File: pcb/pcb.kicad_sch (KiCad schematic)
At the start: 22 parts, among them J1 AVR-ISP-6, SW1 BOOT, SW2 RESET, U1 ATmega328P-P, Y1 Crystal

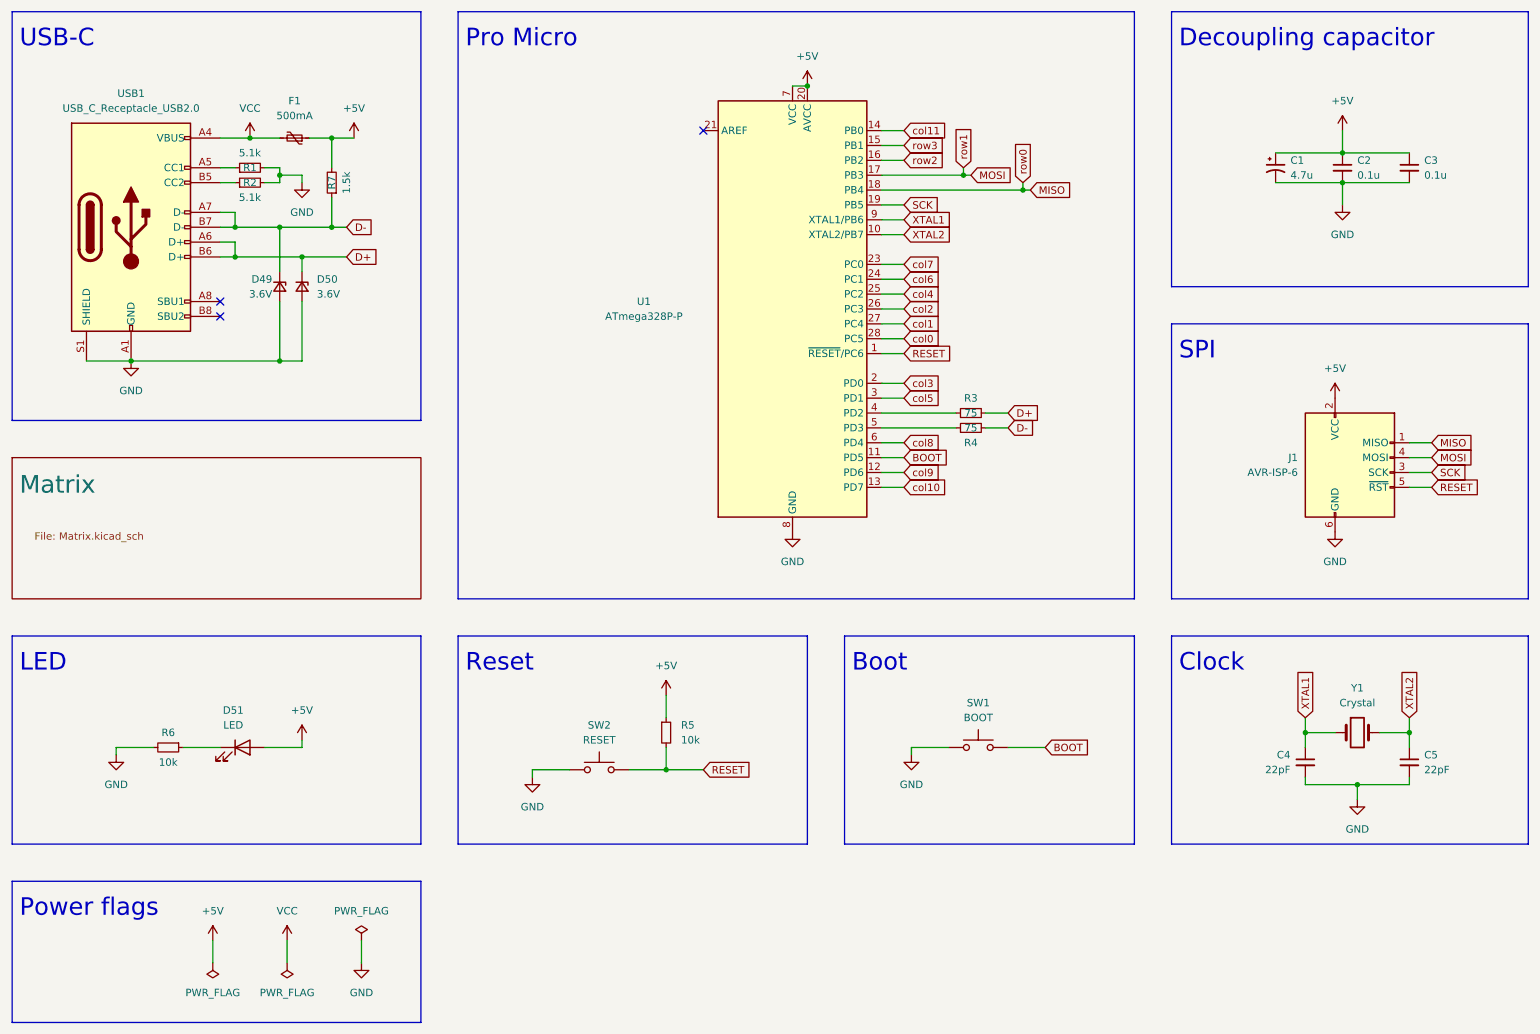
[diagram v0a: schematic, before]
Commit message: 🛠️ Remove unwanted layouts
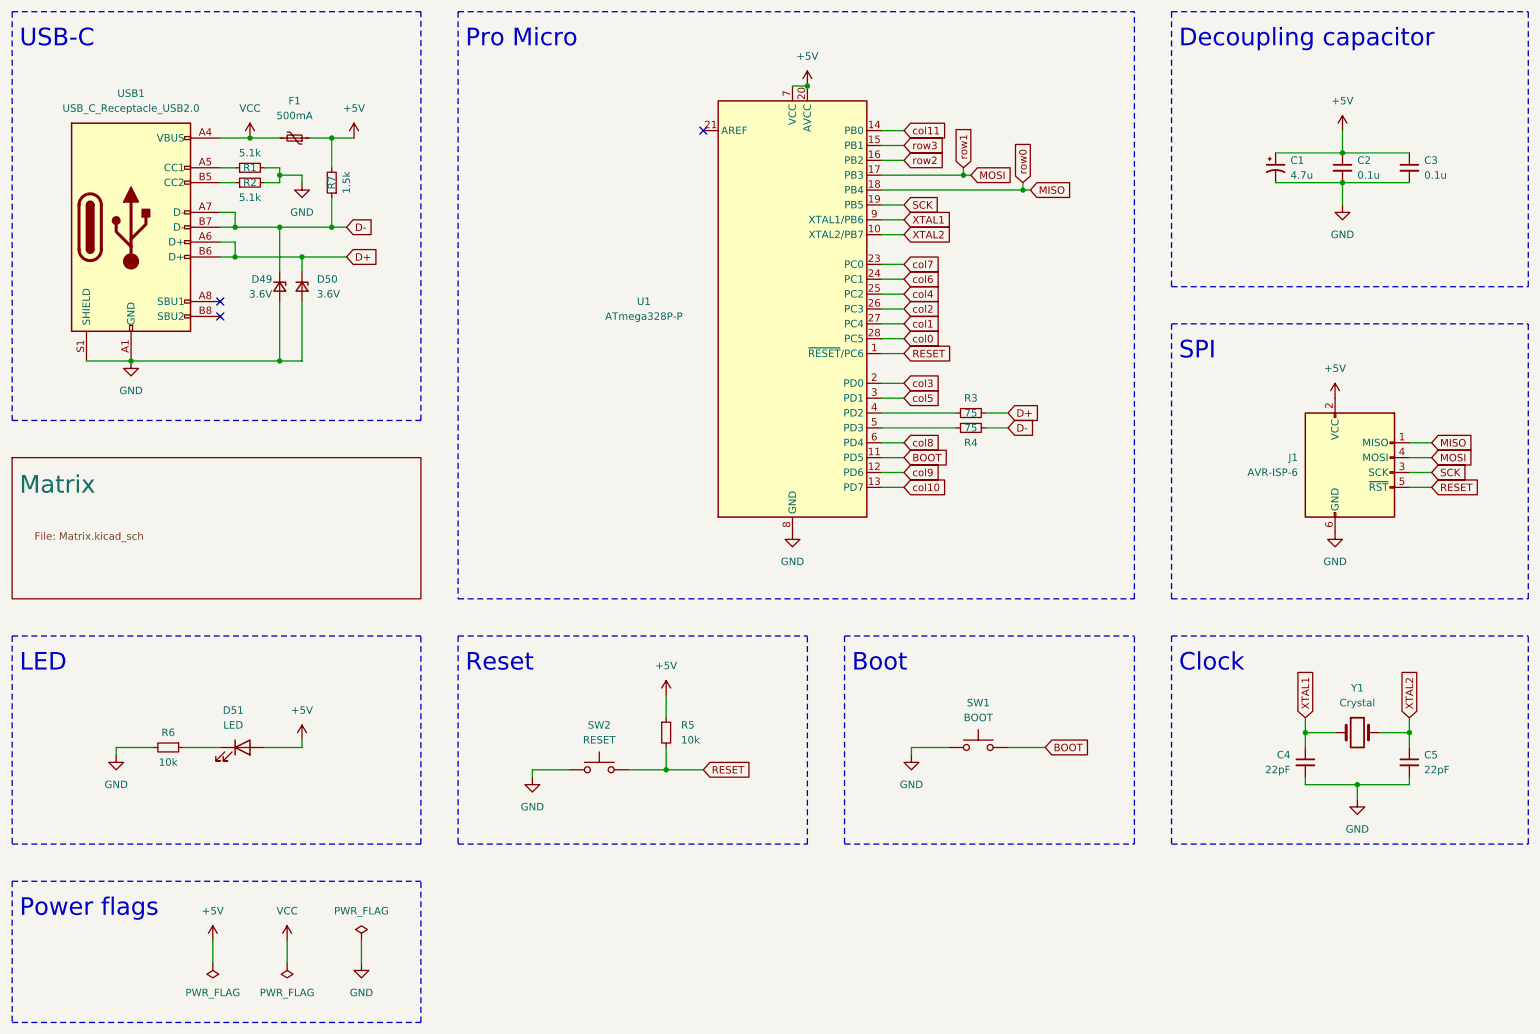
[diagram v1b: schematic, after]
